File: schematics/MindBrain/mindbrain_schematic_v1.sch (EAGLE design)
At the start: 47 parts, among them CON1 POWER, IC1 TL084P, IC2 TL084P

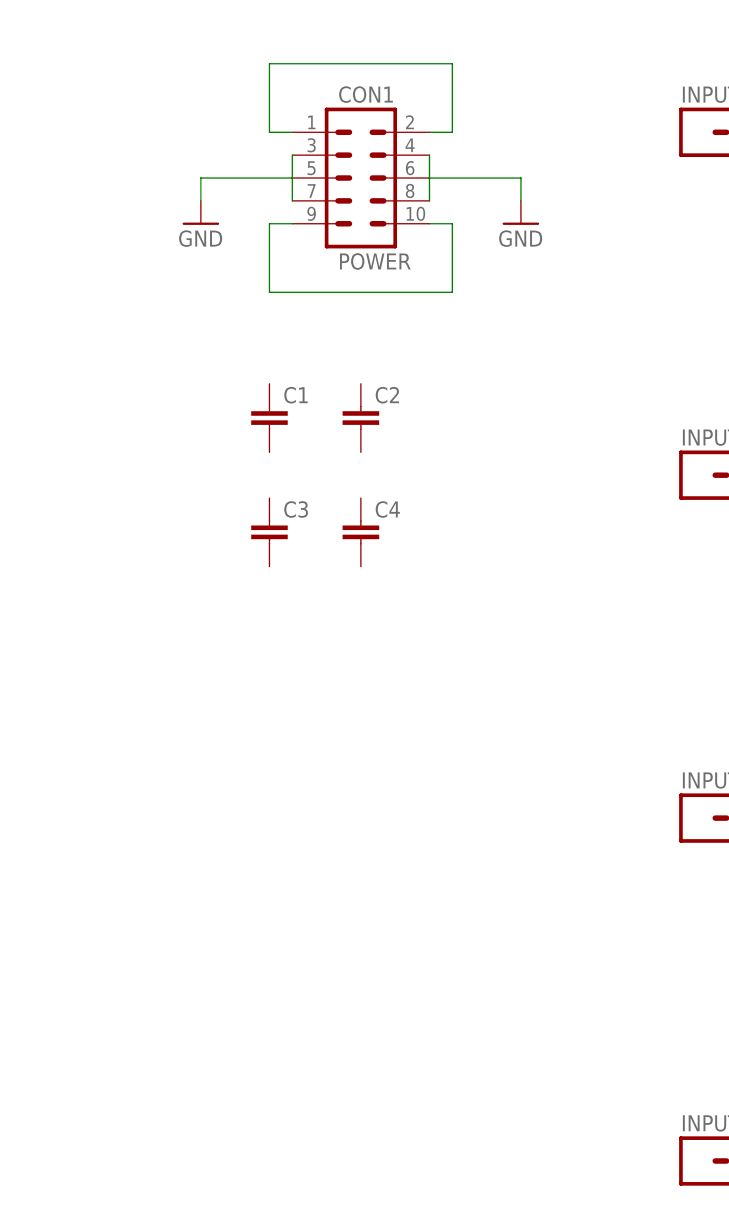
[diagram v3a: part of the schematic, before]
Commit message: made connections to bypass caps in schematic view
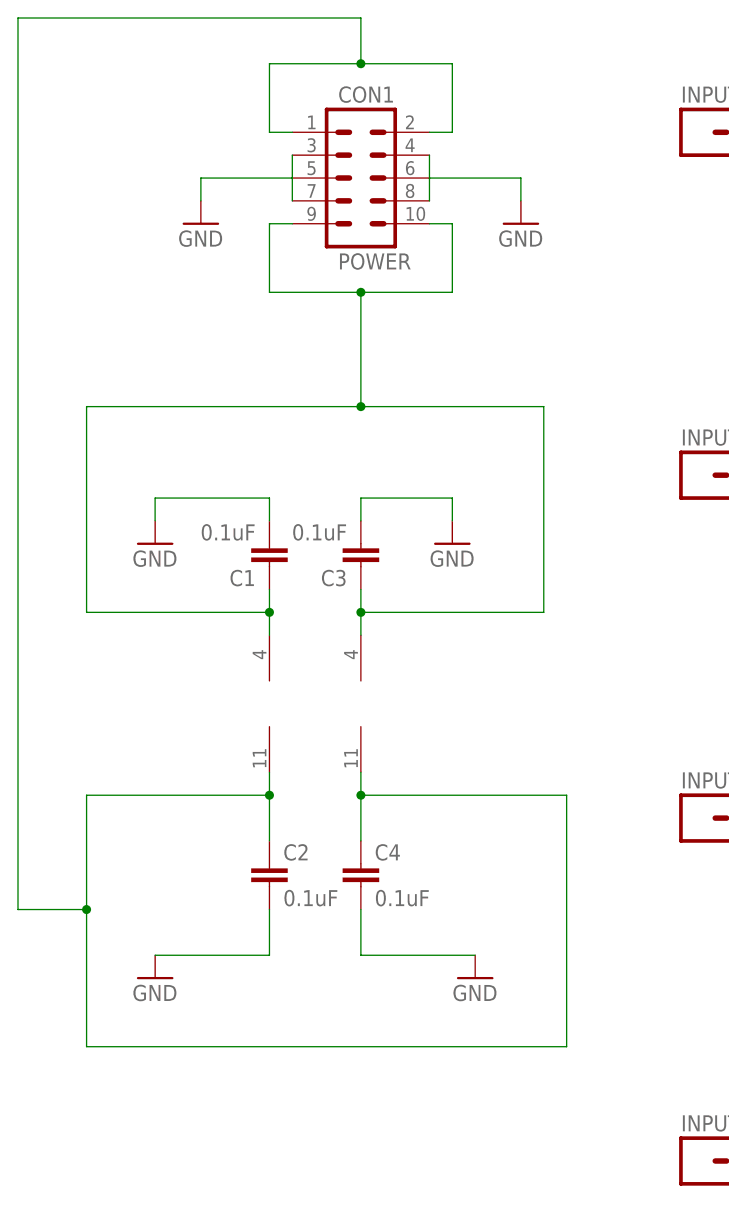
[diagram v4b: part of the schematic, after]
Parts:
- C1, C2, C3, C4: value (none) -> 0.1uF
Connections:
- removed net N$28: CON1.10, CON1.9
- new net N$25: C1.1, C3.1, CON1.10, CON1.9, IC1P.V+, IC2P.V+
- net GND: now also C1.2, C2.2, C3.2, C4.2
- net N$27: now also C2.1, C4.1, IC1P.V-, IC2P.V-
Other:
- moved on the sheet: C1, C2, C3, C4
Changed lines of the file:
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@@
 <part name="GND16" library="SparkFun-Aesthetics" deviceset="GND" device=""/>
 <part name="IC2" library="linear" deviceset="TL084" device="P"/>
-<part name="C1" library="SparkFun-Capacitors" deviceset="CAP" device="KIT"/>
-<part name="C2" library="SparkFun-Capacitors" deviceset="CAP" device="KIT"/>
-<part name="C3" library="SparkFun-Capacitors" deviceset="CAP" device="KIT"/>
-<part name="C4" library="SparkFun-Capacitors" deviceset="CAP" device="KIT"/>
+<part name="C1" library="SparkFun-Capacitors" deviceset="CAP" device="KIT" value="0.1uF"/>
+<part name="C2" library="SparkFun-Capacitors" deviceset="CAP" device="KIT" value="0.1uF"/>
+<part name="C3" library="SparkFun-Capacitors" deviceset="CAP" device="KIT" value="0.1uF"/>
+<part name="C4" library="SparkFun-Capacitors" deviceset="CAP" device="KIT" value="0.1uF"/>
 <part name="CON1" library="SparkFun-Connectors" deviceset="M05X2" device="SHD" value="POWER"/>
 <part name="GND17" library="SparkFun-Aesthetics" deviceset="GND" device=""/>
 <part name="GND18" library="SparkFun-Aesthetics" deviceset="GND" device=""/>
+<part name="GND19" library="SparkFun-Aesthetics" deviceset="GND" device=""/>
+<part name="GND20" library="SparkFun-Aesthetics" deviceset="GND" device=""/>
+<part name="GND21" library="SparkFun-Aesthetics" deviceset="GND" device=""/>
+<part name="GND22" library="SparkFun-Aesthetics" deviceset="GND" device=""/>
 </parts>
 <sheets>
@@
 <instance part="IC2" gate="C" x="88.9" y="7.62"/>
 <instance part="IC2" gate="D" x="88.9" y="-30.48"/>
-<instance part="C1" gate="G$1" x="-55.88" y="53.34"/>
-<instance part="C2" gate="G$1" x="-45.72" y="53.34"/>
-<instance part="C3" gate="G$1" x="-55.88" y="40.64"/>
-<instance part="C4" gate="G$1" x="-45.72" y="40.64"/>
+<instance part="C1" gate="G$1" x="-55.88" y="40.64" rot="R180"/>
+<instance part="C2" gate="G$1" x="-55.88" y="2.54"/>
+<instance part="C3" gate="G$1" x="-45.72" y="40.64" rot="R180"/>
+<instance part="C4" gate="G$1" x="-45.72" y="2.54"/>
 <instance part="CON1" gate="G$1" x="-45.72" y="81.28"/>
 <instance part="GND17" gate="1" x="-27.94" y="76.2"/>
 <instance part="GND18" gate="1" x="-63.5" y="76.2"/>
+<instance part="IC1" gate="P" x="-55.88" y="22.86"/>
+<instance part="IC2" gate="P" x="-45.72" y="22.86"/>
+<instance part="GND19" gate="1" x="-68.58" y="-7.62"/>
+<instance part="GND20" gate="1" x="-33.02" y="-7.62"/>
+<instance part="GND21" gate="1" x="-68.58" y="40.64"/>
+<instance part="GND22" gate="1" x="-35.56" y="40.64"/>
 </instances>
 <busses>
@@
 <wire x1="-63.5" y1="81.28" x2="-63.5" y2="78.74" width="0.1524" layer="91"/>
 </segment>
+<segment>
+<pinref part="GND19" gate="1" pin="GND"/>
+<pinref part="C2" gate="G$1" pin="2"/>
+<wire x1="-68.58" y1="-5.08" x2="-55.88" y2="-5.08" width="0.1524" layer="91"/>
+<wire x1="-55.88" y1="-5.08" x2="-55.88" y2="0" width="0.1524" layer="91"/>
+</segment>
+<segment>
+<pinref part="GND20" gate="1" pin="GND"/>
+<pinref part="C4" gate="G$1" pin="2"/>
+<wire x1="-33.02" y1="-5.08" x2="-45.72" y2="-5.08" width="0.1524" layer="91"/>
+<wire x1="-45.72" y1="-5.08" x2="-45.72" y2="0" width="0.1524" layer="91"/>
+</segment>
+<segment>
+<pinref part="C1" gate="G$1" pin="2"/>
+<wire x1="-55.88" y1="43.18" x2="-55.88" y2="45.72" width="0.1524" layer="91"/>
+<pinref part="GND21" gate="1" pin="GND"/>
+<wire x1="-55.88" y1="45.72" x2="-68.58" y2="45.72" width="0.1524" layer="91"/>
+<wire x1="-68.58" y1="45.72" x2="-68.58" y2="43.18" width="0.1524" layer="91"/>
+</segment>
+<segment>
+<pinref part="C3" gate="G$1" pin="2"/>
+<wire x1="-45.72" y1="43.18" x2="-45.72" y2="45.72" width="0.1524" layer="91"/>
+<pinref part="GND22" gate="1" pin="GND"/>
+<wire x1="-45.72" y1="45.72" x2="-35.56" y2="45.72" width="0.1524" layer="91"/>
+<wire x1="-35.56" y1="45.72" x2="-35.56" y2="43.18" width="0.1524" layer="91"/>
+</segment>
 </net>
 <net name="N$2" class="0">
@@
 <wire x1="-53.34" y1="86.36" x2="-55.88" y2="86.36" width="0.1524" layer="91"/>
 <wire x1="-55.88" y1="86.36" x2="-55.88" y2="93.98" width="0.1524" layer="91"/>
-<wire x1="-55.88" y1="93.98" x2="-35.56" y2="93.98" width="0.1524" layer="91"/>
+<wire x1="-55.88" y1="93.98" x2="-45.72" y2="93.98" width="0.1524" layer="91"/>
+<wire x1="-45.72" y1="93.98" x2="-35.56" y2="93.98" width="0.1524" layer="91"/>
 <wire x1="-35.56" y1="93.98" x2="-35.56" y2="86.36" width="0.1524" layer="91"/>
 <pinref part="CON1" gate="G$1" pin="2"/>
 <wire x1="-35.56" y1="86.36" x2="-38.1" y2="86.36" width="0.1524" layer="91"/>
-</segment>
-</net>
-<net name="N$28" class="0">
-<segment>
+<wire x1="-45.72" y1="93.98" x2="-45.72" y2="99.06" width="0.1524" layer="91"/>
+<wire x1="-45.72" y1="99.06" x2="-83.82" y2="99.06" width="0.1524" layer="91"/>
+<wire x1="-83.82" y1="99.06" x2="-83.82" y2="0" width="0.1524" layer="91"/>
+<pinref part="C2" gate="G$1" pin="1"/>
+<pinref part="IC1" gate="P" pin="V-"/>
+<wire x1="-55.88" y1="7.62" x2="-55.88" y2="12.7" width="0.1524" layer="91"/>
+<wire x1="-55.88" y1="12.7" x2="-55.88" y2="15.24" width="0.1524" layer="91"/>
+<wire x1="-55.88" y1="12.7" x2="-76.2" y2="12.7" width="0.1524" layer="91"/>
+<wire x1="-76.2" y1="12.7" x2="-76.2" y2="0" width="0.1524" layer="91"/>
+<wire x1="-76.2" y1="0" x2="-76.2" y2="-15.24" width="0.1524" layer="91"/>
+<wire x1="-76.2" y1="-15.24" x2="-22.86" y2="-15.24" width="0.1524" layer="91"/>
+<wire x1="-22.86" y1="-15.24" x2="-22.86" y2="12.7" width="0.1524" layer="91"/>
+<pinref part="C4" gate="G$1" pin="1"/>
+<pinref part="IC2" gate="P" pin="V-"/>
+<wire x1="-45.72" y1="7.62" x2="-45.72" y2="12.7" width="0.1524" layer="91"/>
+<wire x1="-45.72" y1="12.7" x2="-45.72" y2="15.24" width="0.1524" layer="91"/>
+<wire x1="-22.86" y1="12.7" x2="-45.72" y2="12.7" width="0.1524" layer="91"/>
+<junction x="-55.88" y="12.7"/>
+<junction x="-45.72" y="12.7"/>
+<wire x1="-83.82" y1="0" x2="-76.2" y2="0" width="0.1524" layer="91"/>
+<junction x="-76.2" y="0"/>
+<junction x="-45.72" y="93.98"/>
+</segment>
+</net>
+<net name="N$25" class="0">
+<segment>
+<pinref part="IC1" gate="P" pin="V+"/>
+<pinref part="C1" gate="G$1" pin="1"/>
+<wire x1="-55.88" y1="35.56" x2="-55.88" y2="33.02" width="0.1524" layer="91"/>
+<wire x1="-55.88" y1="33.02" x2="-55.88" y2="30.48" width="0.1524" layer="91"/>
+<wire x1="-55.88" y1="33.02" x2="-76.2" y2="33.02" width="0.1524" layer="91"/>
+<wire x1="-76.2" y1="33.02" x2="-76.2" y2="55.88" width="0.1524" layer="91"/>
+<pinref part="IC2" gate="P" pin="V+"/>
+<pinref part="C3" gate="G$1" pin="1"/>
+<wire x1="-45.72" y1="35.56" x2="-45.72" y2="33.02" width="0.1524" layer="91"/>
+<wire x1="-45.72" y1="33.02" x2="-45.72" y2="30.48" width="0.1524" layer="91"/>
+<wire x1="-45.72" y1="33.02" x2="-25.4" y2="33.02" width="0.1524" layer="91"/>
+<wire x1="-25.4" y1="33.02" x2="-25.4" y2="55.88" width="0.1524" layer="91"/>
 <pinref part="CON1" gate="G$1" pin="9"/>
 <wire x1="-53.34" y1="76.2" x2="-55.88" y2="76.2" width="0.1524" layer="91"/>
 <wire x1="-55.88" y1="76.2" x2="-55.88" y2="68.58" width="0.1524" layer="91"/>
-<wire x1="-55.88" y1="68.58" x2="-35.56" y2="68.58" width="0.1524" layer="91"/>
+<wire x1="-55.88" y1="68.58" x2="-45.72" y2="68.58" width="0.1524" layer="91"/>
+<wire x1="-45.72" y1="68.58" x2="-35.56" y2="68.58" width="0.1524" layer="91"/>
 <wire x1="-35.56" y1="68.58" x2="-35.56" y2="76.2" width="0.1524" layer="91"/>
 <pinref part="CON1" gate="G$1" pin="10"/>
 <wire x1="-35.56" y1="76.2" x2="-38.1" y2="76.2" width="0.1524" layer="91"/>
-</segment>
-</net>
+<wire x1="-25.4" y1="55.88" x2="-45.72" y2="55.88" width="0.1524" layer="91"/>
+<wire x1="-45.72" y1="55.88" x2="-45.72" y2="68.58" width="0.1524" layer="91"/>
+<wire x1="-76.2" y1="55.88" x2="-45.72" y2="55.88" width="0.1524" layer="91"/>
+<junction x="-45.72" y="55.88"/>
+<junction x="-45.72" y="68.58"/>
+<junction x="-55.88" y="33.02"/>
+<junction x="-45.72" y="33.02"/>
+</segment>
+</net>

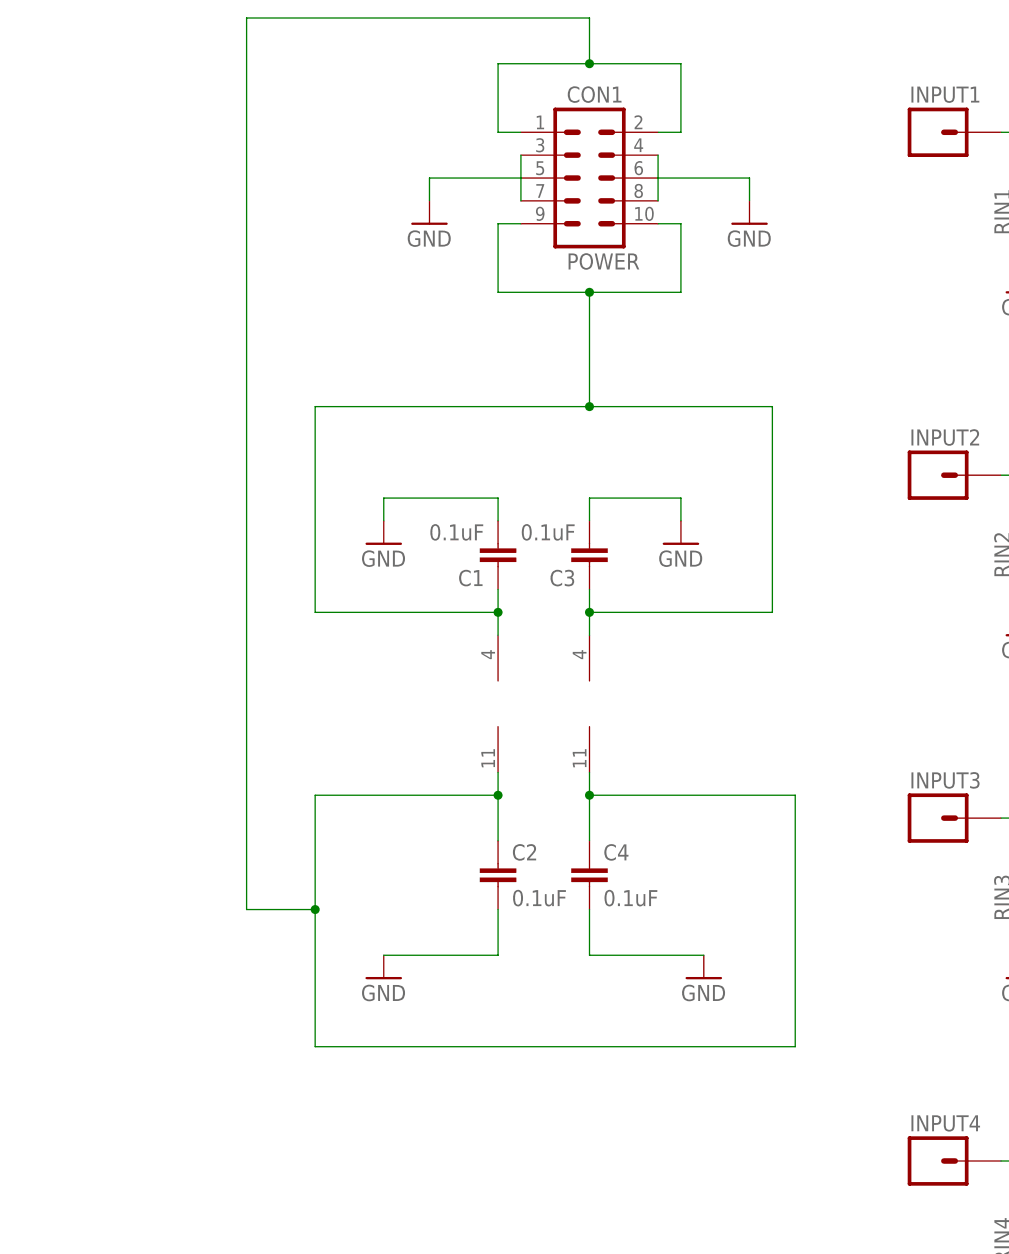
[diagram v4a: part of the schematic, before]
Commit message: added audio input and output grounds
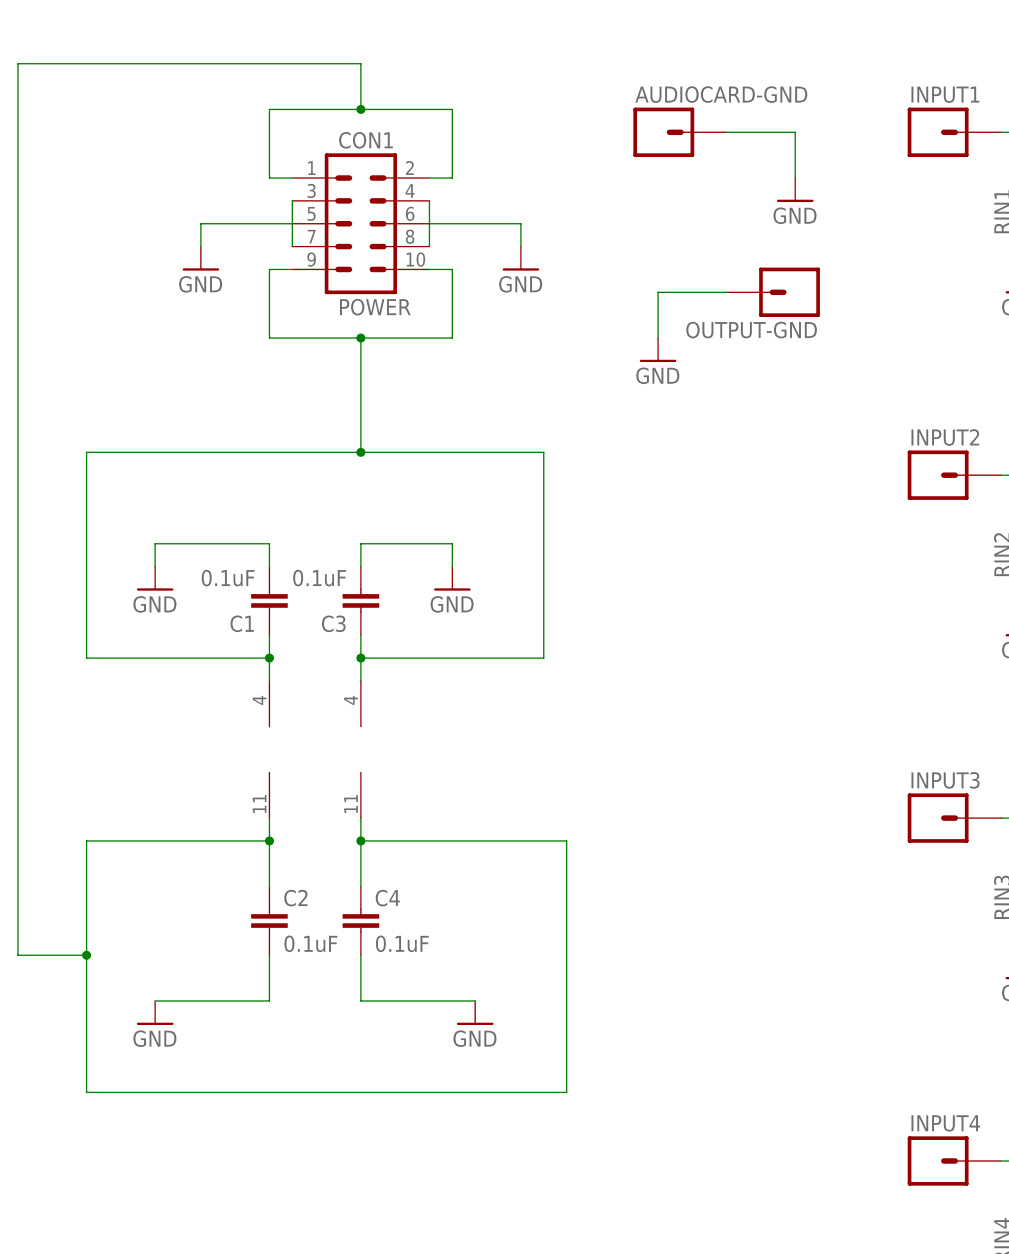
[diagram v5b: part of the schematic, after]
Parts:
- added AUDIOCARD-GND, OUTPUT-GND: M01NOSILK-KIT, SparkFun-Connectors:M01NOSILK-KIT
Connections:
- net GND: now also AUDIOCARD-GND.1, OUTPUT-GND.1
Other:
- moved on the sheet: C1, C2, C3, C4, CON1
